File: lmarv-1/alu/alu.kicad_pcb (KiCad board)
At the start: 4 copper layers, 111.3 x 141 mm, 126 parts, among them J1 Conn_02x03_Odd_Even, J2 Conn_01x01, J3 Conn_01x01, J4 Conn_01x01, P1 dual-pcie-cardedge, Q1 DMP3056L, Q2 DMP3056L, Q3 DMP3056L, U1 74HC590, U10 74LVC541, U11 IS61LV256AL, U12 74LVC541, U13 74LVC541, U14 74LVC541, U15 IS61LV256AL, U16 IS61LV256AL, U17 74LVC541, U18 74LVC541, U19 74LVC541, U2 AT28BV64B-20JU, U20 IS61LV256AL, U21 74LVC541, U22 74LVC541, U23 74LVC541, U24 IS61LV256AL, U25 74LVC541, U26 74LVC541, U27 74LVC541, U28 IS61LV256AL, U29 74LVC541, U3 AT28BV256B-20JU, U30 74LVC541, U31 74LVC541, U32 IS61LV256AL, U33 74LVC541, U34 74LVC541, U35 74LVC541, U36 IS61LV256AL, U37 74LVC541, U38 74LVC541, U39 74LVC541, U4 74HC590, U40 IS61LV256AL, U41 74LVC541, U42 74LVC32, U43 74LVC04, U44 74LVC32, U45 74LVC541, U46 74LVC541, U47 74LVC541, U48 74LVC541, U49 74LVC541, U5 74LVC541, U50 74LVC541, U51 74LVC541, U52 74LVC541, U53 74LVC541, U54 74LVC541, U55 74LVC541, U56 74LVC541, U6 74LVC541, U7 74LVC541, U8 74LVC541, U9 74LVC541

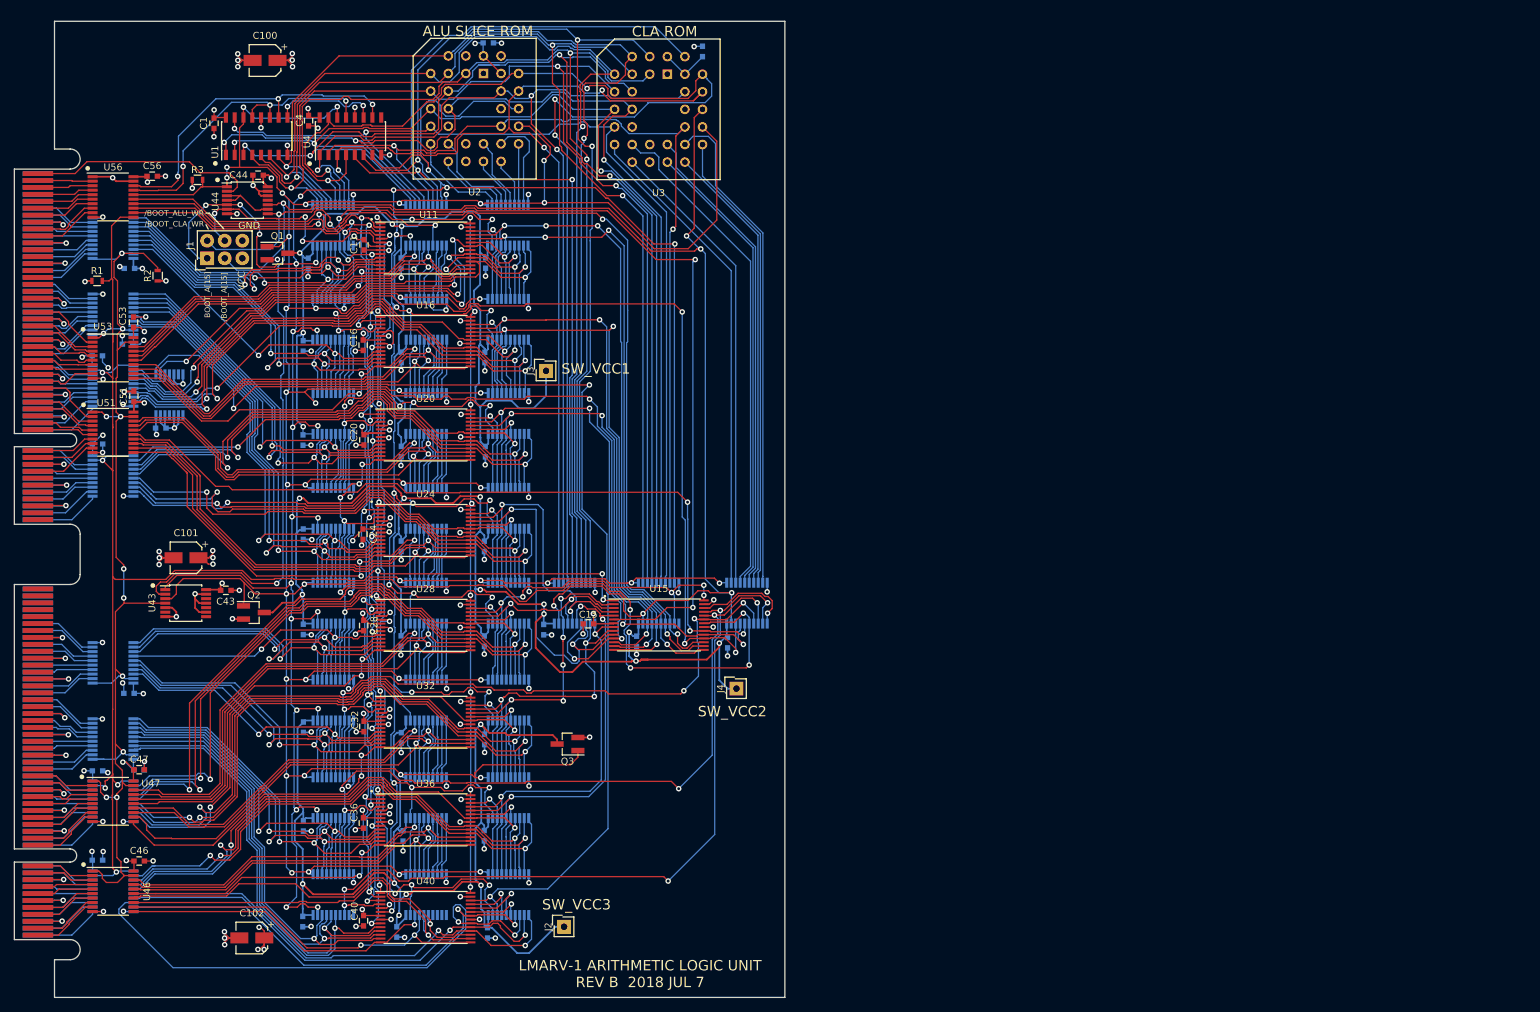
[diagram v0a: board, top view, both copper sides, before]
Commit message: Update alu.py, add some instruction diagrams
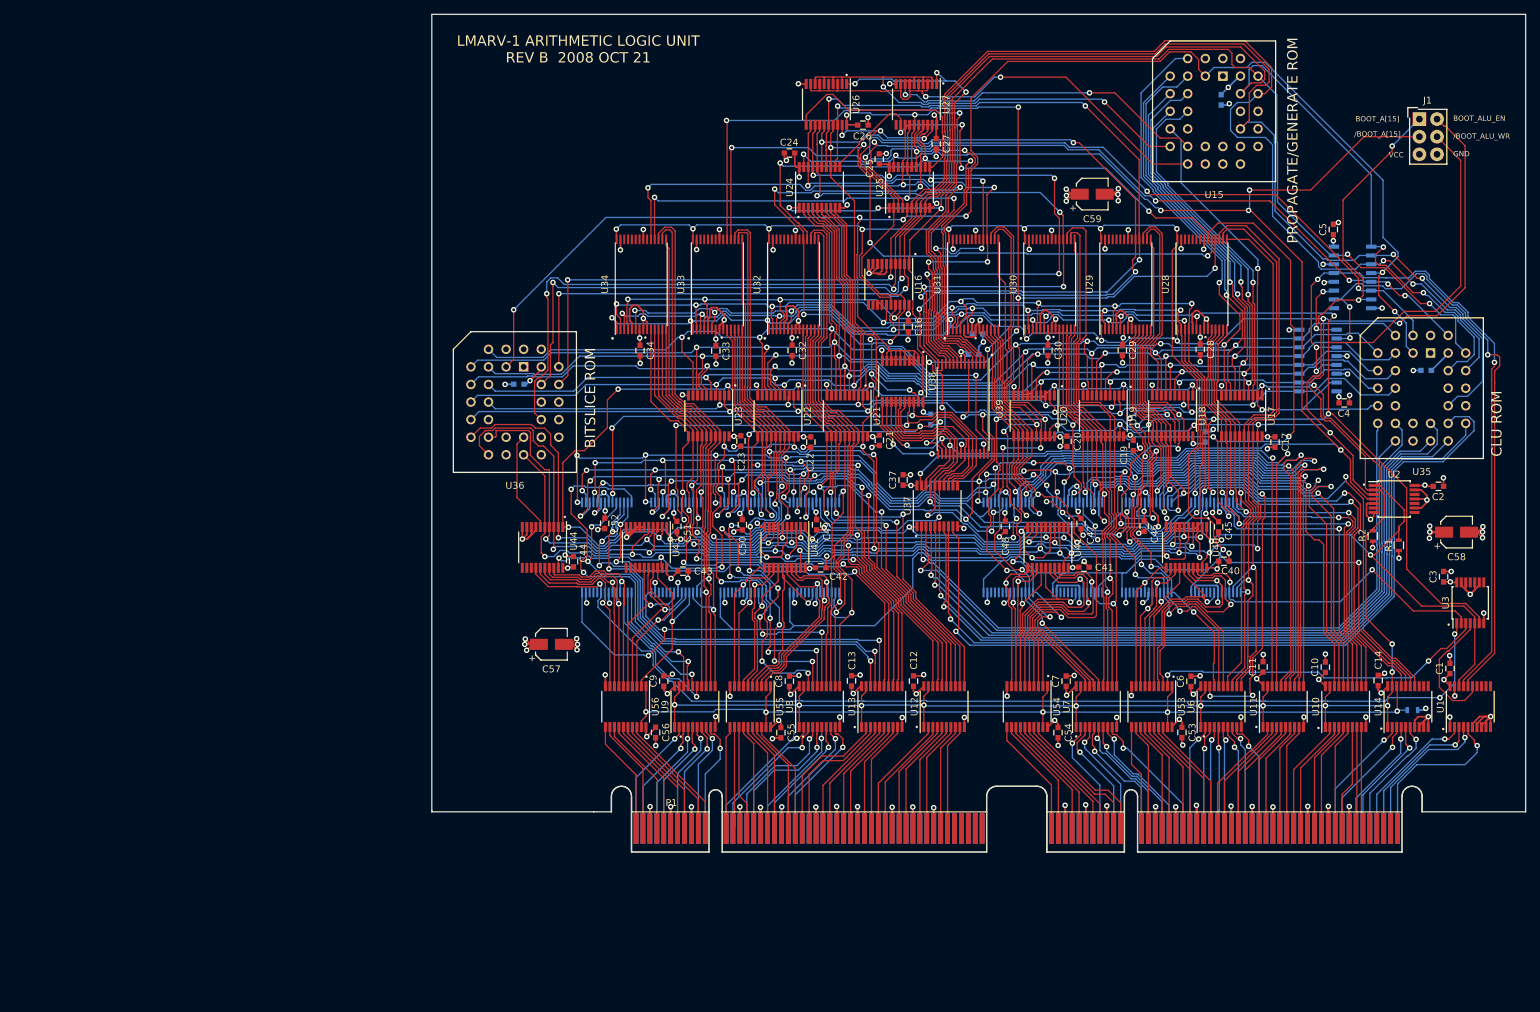
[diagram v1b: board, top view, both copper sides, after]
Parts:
- removed C100, C101, C102: 1u, Capacitors_SMD:CP_Elec_4x4.5
- removed J2, J3, J4: Conn_01x01, Connectors_Samtec:SL-101-X-XX_1x01
- removed Q1, Q2, Q3: DMP3056L, TO_SOT_Packages_SMD:SOT-23_Handsoldering
- added C57: 1u, Capacitors_SMD:CP_Elec_4x4.5, F.Cu at (81.3, 121.0)
- added C58: 1u, Capacitors_SMD:CP_Elec_4x4.5, F.Cu at (212.0, 104.8)
- added C59: 1u, Capacitors_SMD:CP_Elec_4x4.5, F.Cu at (159.4, 56.0)
- C1, C11, C16, C18, C20, C24, C28, C31, C32, C35, C38, C39, C4, C40, C43, C44, C46, C47, C51, C53, C56: value 0u1 -> 100n
- C10, C12, C13, C14, C17, C19, C2, C21, C22, C23, C25, C26, C27, C29, C3, C30, C33, C34, C37, C41, C42, C45, C48, C49, C5, C50, C52, C54, C55, C6, C7, C8, C9: value 0u1 -> 100n; moved to F.Cu
- C15, C36: value 0u1 -> 100n; moved to B.Cu
- P1: value dual-pcie-cardedge -> dual-pcie-cardedge_split; moved to F.Cu
- R3, U4: moved to B.Cu
- U1: value 74HC590 -> 74LVC541; footprint Housings_SOIC:SOIC-16_3.9x9.9mm_Pitch1.27mm -> Housings_SSOP:TSSOP-20_4.4x6.5mm_Pitch0.65mm
- U10, U12, U13, U25, U38, U6, U7, U8, U9: value 74LVC541 -> 74LVC541_a; moved to F.Cu
- U11, U24: value IS61LV256AL -> 74LVC541_a; footprint lmarv:TSOP-I-28_18.4x8mm_Pitch0.55mm -> Housings_SSOP:TSSOP-20_4.4x6.5mm_Pitch0.65mm
- U14, U17, U18, U19, U21, U22, U23, U26, U27, U37, U41, U54, U55: moved to F.Cu
- U15, U36: value IS61LV256AL -> AT28BV64B-20JU; footprint lmarv:TSOP-I-28_18.4x8mm_Pitch0.55mm -> Sockets:PLCC32
- U16, U20, U40: value IS61LV256AL -> 74LVC541; footprint lmarv:TSOP-I-28_18.4x8mm_Pitch0.55mm -> Housings_SSOP:TSSOP-20_4.4x6.5mm_Pitch0.65mm
- U2: value AT28BV64B-20JU -> 74LVC04; footprint Sockets:PLCC32 -> Housings_SSOP:TSSOP-14_4.4x5mm_Pitch0.65mm
- U29, U30, U31, U33, U34, U39: value 74LVC541 -> IS61LV256AL; footprint Housings_SSOP:TSSOP-20_4.4x6.5mm_Pitch0.65mm -> lmarv:TSOP-I-28_18.4x8mm_Pitch0.55mm; moved to F.Cu
- U3: value AT28BV256B-20JU -> 74LVC32; footprint Sockets:PLCC32 -> Housings_SSOP:TSSOP-14_4.4x5mm_Pitch0.65mm
- U35: value 74LVC541 -> AT28BV256B-20JU; footprint Housings_SSOP:TSSOP-20_4.4x6.5mm_Pitch0.65mm -> Sockets:PLCC32; moved to F.Cu
- U42: value 74LVC32 -> 74LVC541; footprint Housings_SSOP:TSSOP-14_4.4x5mm_Pitch0.65mm -> Housings_SSOP:TSSOP-20_4.4x6.5mm_Pitch0.65mm; moved to F.Cu
- U43: value 74LVC04 -> 74LVC541; footprint Housings_SSOP:TSSOP-14_4.4x5mm_Pitch0.65mm -> Housings_SSOP:TSSOP-20_4.4x6.5mm_Pitch0.65mm
- U44: value 74LVC32 -> 74LVC541; footprint Housings_SSOP:TSSOP-14_4.4x5mm_Pitch0.65mm -> Housings_SSOP:TSSOP-20_4.4x6.5mm_Pitch0.65mm
- U45, U48, U49, U50, U52: value 74LVC541 -> IS61LV256AL; footprint Housings_SSOP:TSSOP-20_4.4x6.5mm_Pitch0.65mm -> lmarv:TSOP-I-28_18.4x8mm_Pitch0.55mm
- U46, U47, U51: value 74LVC541 -> IS61LV256AL; footprint Housings_SSOP:TSSOP-20_4.4x6.5mm_Pitch0.65mm -> lmarv:TSOP-I-28_18.4x8mm_Pitch0.55mm; moved to B.Cu
- U5: value 74LVC541 -> 74HC590; footprint Housings_SSOP:TSSOP-20_4.4x6.5mm_Pitch0.65mm -> Housings_SOIC:SOIC-16_3.9x9.9mm_Pitch1.27mm
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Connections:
- C1 pad 2: GND -> GNDREF
- C10 pad 1: /SW_VCC2 -> VCC
- C10 pad 2: GND -> GNDREF
- C11 pad 2: GND -> GNDREF
- C12 pad 1: /SW_VCC1 -> VCC
- C12 pad 2: GND -> GNDREF
- C13 pad 1: /SW_VCC1 -> VCC
- C13 pad 2: GND -> GNDREF
- C14 pad 1: /SW_VCC1 -> VCC
- C14 pad 2: GND -> GNDREF
- C15 pad 2: GND -> GNDREF
- C16 pad 2: GND -> GNDREF
- C17 pad 1: /SW_VCC1 -> VCC
- C17 pad 2: GND -> GNDREF
- C18 pad 1: /SW_VCC1 -> VCC
- C18 pad 2: GND -> GNDREF
- C19 pad 1: /SW_VCC1 -> VCC
- C19 pad 2: GND -> GNDREF
- C2 pad 2: GND -> GNDREF
- C20 pad 2: GND -> GNDREF
- C21 pad 1: /SW_VCC2 -> VCC
- C21 pad 2: GND -> GNDREF
- C22 pad 1: /SW_VCC2 -> VCC
- C22 pad 2: GND -> GNDREF
- C23 pad 1: /SW_VCC2 -> VCC
- C23 pad 2: GND -> GNDREF
- C24 pad 2: GND -> GNDREF
- C25 pad 1: /SW_VCC2 -> VCC
- C25 pad 2: GND -> GNDREF
- C26 pad 1: /SW_VCC2 -> VCC
- C26 pad 2: GND -> GNDREF
- C27 pad 1: /SW_VCC2 -> VCC
- C27 pad 2: GND -> GNDREF
- C28 pad 2: GND -> GNDREF
- C29 pad 1: /SW_VCC3 -> VCC
- C29 pad 2: GND -> GNDREF
- C3 pad 2: GND -> GNDREF
- C30 pad 1: /SW_VCC3 -> VCC
- C30 pad 2: GND -> GNDREF
- C31 pad 1: /SW_VCC3 -> VCC
- C31 pad 2: GND -> GNDREF
- C32 pad 2: GND -> GNDREF
- C33 pad 1: /SW_VCC3 -> VCC
- C33 pad 2: GND -> GNDREF
- C34 pad 1: /SW_VCC3 -> VCC
- C34 pad 2: GND -> GNDREF
- C35 pad 1: /SW_VCC3 -> VCC
- C35 pad 2: GND -> GNDREF
- C36 pad 2: GND -> GNDREF
- C37 pad 1: /SW_VCC3 -> VCC
- C37 pad 2: GND -> GNDREF
- C38 pad 1: /SW_VCC3 -> VCC
- C38 pad 2: GND -> GNDREF
- C39 pad 1: /SW_VCC3 -> VCC
- C39 pad 2: GND -> GNDREF
- C4 pad 2: GND -> GNDREF
- C40 pad 2: GND -> GNDREF
- C41 pad 2: GND -> GNDREF
- C42 pad 2: GND -> GNDREF
- C43 pad 2: GND -> GNDREF
- C44 pad 2: GND -> GNDREF
- C45 pad 2: GND -> GNDREF
- C46 pad 2: GND -> GNDREF
- C47 pad 2: GND -> GNDREF
- C48 pad 2: GND -> GNDREF
- C49 pad 2: GND -> GNDREF
- C5 pad 1: /SW_VCC1 -> VCC
- C5 pad 2: GND -> GNDREF
- C50 pad 2: GND -> GNDREF
- C51 pad 2: GND -> GNDREF
- C52 pad 2: GND -> GNDREF
- C53 pad 2: GND -> GNDREF
- C54 pad 2: GND -> GNDREF
- C55 pad 2: GND -> GNDREF
- C56 pad 2: GND -> GNDREF
- C6 pad 1: /SW_VCC1 -> VCC
- C6 pad 2: GND -> GNDREF
- C7 pad 1: /SW_VCC1 -> VCC
- C7 pad 2: GND -> GNDREF
- C8 pad 1: /SW_VCC2 -> VCC
- C8 pad 2: GND -> GNDREF
- C9 pad 1: /SW_VCC2 -> VCC
- C9 pad 2: GND -> GNDREF
- J1 pad 2: /~BOOT_CLA_WR -> /BOOT_ALU_EN
- J1 pad 6: GND -> GNDREF
- P1 pad 101: GND -> GNDREF
- P1 pad 107: GND -> GNDREF
- P1 pad 112: GND -> GNDREF
- P1 pad 118: GND -> GNDREF
- P1 pad 123: GND -> GNDREF
- P1 pad 129: GND -> GNDREF
- P1 pad 134: GND -> GNDREF
- P1 pad 14: GND -> GNDREF
- P1 pad 140: GND -> GNDREF
- P1 pad 150: GND -> GNDREF
- P1 pad 156: GND -> GNDREF
- P1 pad 161: GND -> GNDREF
- P1 pad 167: GND -> GNDREF
- P1 pad 172: GND -> GNDREF
- P1 pad 178: GND -> GNDREF
- P1 pad 183: GND -> GNDREF
- P1 pad 189: GND -> GNDREF
- P1 pad 196: /~BOOT_WR -> /~BOOT_WR'
- P1 pad 20: GND -> GNDREF
- P1 pad 25: GND -> GNDREF
- P1 pad 3: GND -> GNDREF
- P1 pad 31: GND -> GNDREF
- P1 pad 36: GND -> GNDREF
- P1 pad 42: GND -> GNDREF
- P1 pad 52: GND -> GNDREF
- P1 pad 58: GND -> GNDREF
- P1 pad 63: GND -> GNDREF
- P1 pad 69: GND -> GNDREF
- P1 pad 74: GND -> GNDREF
- P1 pad 80: GND -> GNDREF
- P1 pad 85: GND -> GNDREF
- P1 pad 9: GND -> GNDREF
- P1 pad 91: GND -> GNDREF
- R1 pad 2: /~alu_oe -> /~BOOT_ALU_EN
- R2 pad 1: VCC -> /BOOT_ALU_EN
- R2 pad 2: /BOOT_ALU_EN -> GNDREF
- R3 pad 2: /~BOOT_ALU_EN -> /~alu_oe
- U1 pad 1: /BOOT_A[1] -> GNDREF
- U1 pad 10: /~BOOT_RST -> GNDREF
- U1 pad 11: /BOOT_CLK -> Net-(U1-Pad11)
- U1 pad 12: GND -> Net-(U1-Pad12)
- U1 pad 13: /BOOT_CLK -> Net-(U1-Pad13)
- U1 pad 14: /~BOOT_ALU_EN -> Net-(U1-Pad14)
- U1 pad 15: /BOOT_A[0] -> /~BOOT_WR
- U1 pad 16: VCC -> /~BOOT_RST
- U1 pad 2: /BOOT_A[2] -> /~BOOT_ALU_EN'
- U1 pad 3: /BOOT_A[3] -> /BOOT_CLK'
- U1 pad 4: /BOOT_A[4] -> /~BOOT_RST'
- U1 pad 5: /BOOT_A[5] -> /~BOOT_WR'
- U1 pad 6: /BOOT_A[6] -> GNDREF
- U1 pad 7: /BOOT_A[7] -> GNDREF
- U1 pad 8: GND -> GNDREF
- U1 pad 9: /~BOOT_RCO -> GNDREF
- U10 pad 1: /~BOOT_ALU_EN -> /BOOT_ALU_EN
- U10 pad 10: GND -> GNDREF
- U10 pad 11: Net-(U10-Pad11) -> /rs2b[0]
- U10 pad 12: /cin[7] -> /rs2b[1]
- U10 pad 13: /cin[6] -> /rs2b[2]
- U10 pad 14: /cin[5] -> /rs2b[3]
- U10 pad 15: /cin[4] -> /rs2b[4]
- U10 pad 16: /cin[3] -> /rs2b[5]
- U10 pad 17: /cin[2] -> /rs2b[6]
- U10 pad 18: /cin[1] -> /rs2b[7]
- U10 pad 19: /~BOOT_A[15] -> /BOOT_ALU_EN
- U10 pad 2: /CLA_D0 -> /rs2[7]
- U10 pad 20: /SW_VCC2 -> VCC
- U10 pad 3: /CLA_D1 -> /rs2[6]
- U10 pad 4: /CLA_D2 -> /rs2[5]
- U10 pad 5: /CLA_D3 -> /rs2[4]
- U10 pad 6: /CLA_D4 -> /rs2[3]
- U10 pad 7: /CLA_D5 -> /rs2[2]
- U10 pad 8: /CLA_D6 -> /rs2[1]
- U10 pad 9: /CLA_D7 -> /rs2[0]
- U11 pad 1: GND -> /BOOT_ALU_EN
- U11 pad 10: /rs1b[0] -> GNDREF
- U11 pad 11: /rdb[0]' -> /rs2b[8]
- U11 pad 12: /rdb[1] -> /rs2b[9]
- U11 pad 13: /rdb[2] -> /rs2b[10]
- U11 pad 14: GND -> /rs2b[11]
- U11 pad 15: /rdb[3] -> /rs2b[12]
- U11 pad 16: /cout[0] -> /rs2b[13]
- U11 pad 17: /p[0] -> /rs2b[14]
- U11 pad 18: /g[0] -> /rs2b[15]
- U11 pad 19: /lt[0] -> /BOOT_ALU_EN
- U11 pad 2: /alu_f[3] -> /rs2[15]
- U11 pad 20: GND -> VCC
- U11 pad 3: /rs2b[3] -> /rs2[14]
- U11 pad 4: /rs2b[2] -> /rs2[13]
- U11 pad 5: /rs2b[1] -> /rs2[12]
- U11 pad 6: /rs2b[0] -> /rs2[11]
- U11 pad 7: /rs1b[3] -> /rs2[10]
- U11 pad 8: /rs1b[2] -> /rs2[9]
- U11 pad 9: /rs1b[1] -> /rs2[8]
- U12 pad 1: /~BOOT_ALU_EN -> /BOOT_ALU_EN
- U12 pad 10: GND -> GNDREF
- U12 pad 11: Net-(U12-Pad11) -> /rs2b[16]
- U12 pad 12: Net-(U12-Pad12) -> /rs2b[17]
- U12 pad 13: /cin[1] -> /rs2b[18]
- U12 pad 14: Net-(U12-Pad14) -> /rs2b[19]
- U12 pad 15: /rs2b[7] -> /rs2b[20]
- U12 pad 16: /rs2b[6] -> /rs2b[21]
- U12 pad 17: /rs2b[5] -> /rs2b[22]
- U12 pad 18: /rs2b[4] -> /rs2b[23]
- U12 pad 19: /BOOT_A[15] -> /BOOT_ALU_EN
- U12 pad 2: /rs2b[0] -> /rs2[23]
- U12 pad 20: /SW_VCC1 -> VCC
- U12 pad 3: /rs2b[1] -> /rs2[22]
- U12 pad 4: /rs2b[2] -> /rs2[21]
- U12 pad 5: /rs2b[3] -> /rs2[20]
- U12 pad 6: GND -> /rs2[19]
- U12 pad 7: /cin[0] -> /rs2[18]
- U12 pad 8: GND -> /rs2[17]
- U12 pad 9: GND -> /rs2[16]
- U13 pad 1: /~BOOT_ALU_EN -> /BOOT_ALU_EN
- U13 pad 10: GND -> GNDREF
- U13 pad 11: Net-(U13-Pad11) -> /rs2b[24]
- U13 pad 12: Net-(U13-Pad12) -> /rs2b[25]
- U13 pad 13: Net-(U13-Pad13) -> /rs2b[26]
- U13 pad 14: Net-(U13-Pad14) -> /rs2b[27]
- U13 pad 15: /rs1b[4] -> /rs2b[28]
- U13 pad 16: /rs1b[5] -> /rs2b[29]
- U13 pad 17: /rs1b[6] -> /rs2b[30]
- U13 pad 18: /rs1b[7] -> /rs2b[31]
- U13 pad 19: /BOOT_A[15] -> /BOOT_ALU_EN
- U13 pad 2: /rs1b[3] -> /rs2[31]
- U13 pad 20: /SW_VCC1 -> VCC
- U13 pad 3: /rs1b[2] -> /rs2[30]
- U13 pad 4: /rs1b[1] -> /rs2[29]
- U13 pad 5: /rs1b[0] -> /rs2[28]
- U13 pad 6: GND -> /rs2[27]
- U13 pad 7: Net-(U13-Pad7) -> /rs2[26]
- U13 pad 8: Net-(U13-Pad8) -> /rs2[25]
- U13 pad 9: Net-(U13-Pad9) -> /rs2[24]
- U14 pad 1: /~BOOT_ALU_EN -> /BOOT_ALU_EN
- U14 pad 10: GND -> GNDREF
- U14 pad 11: /rdb[4] -> Net-(U14-Pad11)
- U14 pad 12: /rdb[5] -> Net-(U14-Pad12)
- U14 pad 13: /rdb[6] -> Net-(U14-Pad13)
- U14 pad 14: /rdb[7] -> /alu_f[3]
- U14 pad 15: /cout[1] -> /alu_f[2]
- U14 pad 16: /p[1] -> /alu_f[1]
- U14 pad 17: /g[1] -> /alu_f[0]
- U14 pad 18: /lt[1] -> /~alu_oe
- U14 pad 19: /BOOT_A[15] -> /BOOT_ALU_EN
- U14 pad 2: /lt[0] -> /~alu_oe'
- U14 pad 20: /SW_VCC1 -> VCC
- U14 pad 3: /g[0] -> /f[0]
- U14 pad 4: /p[0] -> /f[1]
- U14 pad 5: /cout[0] -> /f[2]
- U14 pad 6: /rdb[3] -> /f[3]
- U14 pad 7: /rdb[2] -> GNDREF
- U14 pad 8: /rdb[1] -> GNDREF
- U14 pad 9: /rdb[0]' -> GNDREF
- U15 pad 1: /g[6] -> Net-(U15-Pad1)
- U15 pad 10: /cin[0] -> /BOOT_A[1]
- U15 pad 11: /cin[1] -> /BOOT_A[0]
- U15 pad 12: /cin[2] -> Net-(U15-Pad12)
- U15 pad 13: /cin[3] -> /SLICE1_G
- U15 pad 14: GND -> /SLICE1_P
- U15 pad 15: /cin[4] -> /SLICE1_CIN
- U15 pad 16: /cin[5] -> GNDREF
- U15 pad 17: /cin[6] -> Net-(U15-Pad17)
- U15 pad 18: /cin[7] -> Net-(U15-Pad18)
- U15 pad 19: Net-(U10-Pad11) -> Net-(U15-Pad19)
- U15 pad 2: /g[5] -> Net-(U15-Pad2)
- U15 pad 20: GND -> Net-(U15-Pad20)
- U15 pad 21: /g[4] -> Net-(U15-Pad21)
- U15 pad 22: /~alu_oe -> Net-(U15-Pad22)
- U15 pad 23: /p[5] -> GNDREF
- U15 pad 24: /p[4] -> /BOOT_A[10]
- U15 pad 25: /g[3] -> GNDREF
- U15 pad 26: /p[6] -> Net-(U15-Pad26)
- U15 pad 27: /~BOOT_CLA_WR -> /BOOT_A[11]
- U15 pad 28: VCC -> /BOOT_A[9]
- U15 pad 3: /p[3] -> /BOOT_A[12]
- U15 pad 4: /g[2] -> /BOOT_A[7]
- U15 pad 5: /p[2] -> /BOOT_A[6]
- U15 pad 6: /g[1] -> /BOOT_A[5]
- U15 pad 7: /p[1] -> /BOOT_A[4]
- U15 pad 8: /g[0] -> /BOOT_A[3]
- U15 pad 9: /p[0] -> /BOOT_A[2]
- U16 pad 1: GND -> /~BOOT_ALU_EN
- U16 pad 10: /rs1b[4] -> GNDREF
- U16 pad 11: /rdb[4] -> Net-(U16-Pad11)
- U16 pad 12: /rdb[5] -> Net-(U16-Pad12)
- U16 pad 13: /rdb[6] -> Net-(U16-Pad13)
- U16 pad 14: GND -> Net-(U16-Pad14)
- U16 pad 15: /rdb[7] -> /alu_f[3]
- U16 pad 16: /cout[1] -> /alu_f[2]
- U16 pad 17: /p[1] -> /alu_f[1]
- U16 pad 18: /g[1] -> /alu_f[0]
- U16 pad 19: /lt[1] -> /BOOT_A[15]
- U16 pad 2: /alu_f[3] -> /BOOT_A[8]
- U16 pad 20: GND -> VCC
- U16 pad 3: /rs2b[7] -> /BOOT_A[9]
- U16 pad 4: /rs2b[6] -> /BOOT_A[10]
- U16 pad 5: /rs2b[5] -> /BOOT_A[11]
- U16 pad 6: /rs2b[4] -> GNDREF
- U16 pad 7: /rs1b[7] -> GNDREF
- U16 pad 8: /rs1b[6] -> GNDREF
- U16 pad 9: /rs1b[5] -> GNDREF
- U17 pad 10: GND -> GNDREF
- U17 pad 11: Net-(U17-Pad11) -> /rs2b[3]
- U17 pad 12: Net-(U17-Pad12) -> /rs2b[2]
- U17 pad 13: /cin[2] -> /rs2b[1]
- U17 pad 14: Net-(U17-Pad14) -> /rs2b[0]
- U17 pad 15: /rs2b[11] -> /rs1b[3]
- U17 pad 16: /rs2b[10] -> /rs1b[2]
- U17 pad 17: /rs2b[9] -> /rs1b[1]
- U17 pad 18: /rs2b[8] -> /rs1b[0]
- U17 pad 2: /rs2b[4] -> /BOOT_A[0]
- U17 pad 20: /SW_VCC1 -> VCC
- U17 pad 3: /rs2b[5] -> /BOOT_A[1]
- U17 pad 4: /rs2b[6] -> /BOOT_A[2]
- U17 pad 5: /rs2b[7] -> /BOOT_A[3]
- U17 pad 6: Net-(U12-Pad14) -> /BOOT_A[4]
- U17 pad 7: /cin[1] -> /BOOT_A[5]
- U17 pad 8: Net-(U12-Pad12) -> /BOOT_A[6]
- U17 pad 9: Net-(U12-Pad11) -> /BOOT_A[7]
- U18 pad 10: GND -> GNDREF
- U18 pad 11: Net-(U18-Pad11) -> /rs2b[7]
- U18 pad 12: Net-(U18-Pad12) -> /rs2b[6]
- U18 pad 13: Net-(U18-Pad13) -> /rs2b[5]
- U18 pad 14: Net-(U18-Pad14) -> /rs2b[4]
- U18 pad 15: /rs1b[8] -> /rs1b[7]
- U18 pad 16: /rs1b[9] -> /rs1b[6]
- U18 pad 17: /rs1b[10] -> /rs1b[5]
- U18 pad 18: /rs1b[11] -> /rs1b[4]
- U18 pad 2: /rs1b[7] -> /BOOT_A[0]
- U18 pad 20: /SW_VCC1 -> VCC
- U18 pad 3: /rs1b[6] -> /BOOT_A[1]
- U18 pad 4: /rs1b[5] -> /BOOT_A[2]
- U18 pad 5: /rs1b[4] -> /BOOT_A[3]
- U18 pad 6: Net-(U13-Pad14) -> /BOOT_A[4]
- U18 pad 7: Net-(U13-Pad13) -> /BOOT_A[5]
- U18 pad 8: Net-(U13-Pad12) -> /BOOT_A[6]
- U18 pad 9: Net-(U13-Pad11) -> /BOOT_A[7]
- U19 pad 10: GND -> GNDREF
- U19 pad 11: /rdb[8] -> /rs2b[11]
- U19 pad 12: /rdb[9] -> /rs2b[10]
- U19 pad 13: /rdb[10] -> /rs2b[9]
- U19 pad 14: /rdb[11] -> /rs2b[8]
- U19 pad 15: /cout[2] -> /rs1b[11]
- U19 pad 16: /p[2] -> /rs1b[10]
- U19 pad 17: /g[2] -> /rs1b[9]
- U19 pad 18: /lt[2] -> /rs1b[8]
- U19 pad 2: /lt[1] -> /BOOT_A[0]
- U19 pad 20: /SW_VCC1 -> VCC
- U19 pad 3: /g[1] -> /BOOT_A[1]
- U19 pad 4: /p[1] -> /BOOT_A[2]
- U19 pad 5: /cout[1] -> /BOOT_A[3]
- U19 pad 6: /rdb[7] -> /BOOT_A[4]
- U19 pad 7: /rdb[6] -> /BOOT_A[5]
- U19 pad 8: /rdb[5] -> /BOOT_A[6]
- U19 pad 9: /rdb[4] -> /BOOT_A[7]
- U2 pad 1: Net-(U2-Pad1) -> /~BOOT_ALU_EN
- U2 pad 10: /BOOT_A[1] -> Net-(U2-Pad10)
- U2 pad 11: /BOOT_A[0] -> GNDREF
- U2 pad 13: /SLICE_D0 -> GNDREF
- U2 pad 14: /SLICE_D1 -> VCC
- U2 pad 2: Net-(U2-Pad2) -> /BOOT_ALU_EN
- U2 pad 3: /BOOT_A[12] -> /BOOT_A[15]
- U2 pad 4: /BOOT_A[7] -> /~BOOT_A[15]
- U2 pad 5: /BOOT_A[6] -> GNDREF
- U2 pad 6: /BOOT_A[5] -> Net-(U2-Pad6)
- U2 pad 7: /BOOT_A[4] -> GNDREF
- U2 pad 8: /BOOT_A[3] -> Net-(U2-Pad8)
- U2 pad 9: /BOOT_A[2] -> GNDREF
- U20 pad 1: GND -> /~BOOT_ALU_EN
- U20 pad 10: /rs1b[8] -> GNDREF
- U20 pad 11: /rdb[8] -> /rs2b[15]
- U20 pad 12: /rdb[9] -> /rs2b[14]
- U20 pad 13: /rdb[10] -> /rs2b[13]
- U20 pad 14: GND -> /rs2b[12]
- U20 pad 15: /rdb[11] -> /rs1b[15]
- U20 pad 16: /cout[2] -> /rs1b[14]
- U20 pad 17: /p[2] -> /rs1b[13]
- U20 pad 18: /g[2] -> /rs1b[12]
- U20 pad 19: /lt[2] -> /BOOT_A[15]
- U20 pad 2: /alu_f[3] -> /BOOT_A[0]
- U20 pad 20: GND -> VCC
- U20 pad 3: /rs2b[11] -> /BOOT_A[1]
- U20 pad 4: /rs2b[10] -> /BOOT_A[2]
- U20 pad 5: /rs2b[9] -> /BOOT_A[3]
- U20 pad 6: /rs2b[8] -> /BOOT_A[4]
- U20 pad 7: /rs1b[11] -> /BOOT_A[5]
- U20 pad 8: /rs1b[10] -> /BOOT_A[6]
- U20 pad 9: /rs1b[9] -> /BOOT_A[7]
- U21 pad 10: GND -> GNDREF
- U21 pad 11: Net-(U21-Pad11) -> /rs2b[19]
- U21 pad 12: Net-(U21-Pad12) -> /rs2b[18]
- U21 pad 13: /cin[3] -> /rs2b[17]
- U21 pad 14: Net-(U21-Pad14) -> /rs2b[16]
- U21 pad 15: /rs2b[15] -> /rs1b[19]
- U21 pad 16: /rs2b[14] -> /rs1b[18]
- U21 pad 17: /rs2b[13] -> /rs1b[17]
- U21 pad 18: /rs2b[12] -> /rs1b[16]
- U21 pad 2: /rs2b[8] -> /BOOT_A[0]
- U21 pad 20: /SW_VCC2 -> VCC
- U21 pad 3: /rs2b[9] -> /BOOT_A[1]
- U21 pad 4: /rs2b[10] -> /BOOT_A[2]
- U21 pad 5: /rs2b[11] -> /BOOT_A[3]
- U21 pad 6: Net-(U17-Pad14) -> /BOOT_A[4]
- U21 pad 7: /cin[2] -> /BOOT_A[5]
- U21 pad 8: Net-(U17-Pad12) -> /BOOT_A[6]
- U21 pad 9: Net-(U17-Pad11) -> /BOOT_A[7]
- U22 pad 10: GND -> GNDREF
- U22 pad 11: Net-(U22-Pad11) -> /rs2b[23]
- U22 pad 12: Net-(U22-Pad12) -> /rs2b[22]
- U22 pad 13: Net-(U22-Pad13) -> /rs2b[21]
- U22 pad 14: Net-(U22-Pad14) -> /rs2b[20]
- U22 pad 15: /rs1b[12] -> /rs1b[23]
- U22 pad 16: /rs1b[13] -> /rs1b[22]
- U22 pad 17: /rs1b[14] -> /rs1b[21]
- U22 pad 18: /rs1b[15] -> /rs1b[20]
- U22 pad 2: /rs1b[11] -> /BOOT_A[0]
- U22 pad 20: /SW_VCC2 -> VCC
- U22 pad 3: /rs1b[10] -> /BOOT_A[1]
- U22 pad 4: /rs1b[9] -> /BOOT_A[2]
- U22 pad 5: /rs1b[8] -> /BOOT_A[3]
- U22 pad 6: Net-(U18-Pad14) -> /BOOT_A[4]
- U22 pad 7: Net-(U18-Pad13) -> /BOOT_A[5]
- U22 pad 8: Net-(U18-Pad12) -> /BOOT_A[6]
- U22 pad 9: Net-(U18-Pad11) -> /BOOT_A[7]
- U23 pad 10: GND -> GNDREF
- U23 pad 11: /rdb[12] -> /rs2b[27]
- U23 pad 12: /rdb[13] -> /rs2b[26]
- U23 pad 13: /rdb[14] -> /rs2b[25]
- U23 pad 14: /rdb[15] -> /rs2b[24]
- U23 pad 15: /cout[3] -> /rs1b[27]
- U23 pad 16: /p[3] -> /rs1b[26]
- U23 pad 17: /g[3] -> /rs1b[25]
- U23 pad 18: /lt[3] -> /rs1b[24]
- U23 pad 2: /lt[2] -> /BOOT_A[0]
- U23 pad 20: /SW_VCC2 -> VCC
- U23 pad 3: /g[2] -> /BOOT_A[1]
- U23 pad 4: /p[2] -> /BOOT_A[2]
- U23 pad 5: /cout[2] -> /BOOT_A[3]
- U23 pad 6: /rdb[11] -> /BOOT_A[4]
- U23 pad 7: /rdb[10] -> /BOOT_A[5]
- U23 pad 8: /rdb[9] -> /BOOT_A[6]
- U23 pad 9: /rdb[8] -> /BOOT_A[7]
- U24 pad 1: GND -> /~BOOT_ALU_EN
- U24 pad 10: /rs1b[12] -> GNDREF
- U24 pad 11: /rdb[12] -> /cin[0]
- U24 pad 12: /rdb[13] -> /g[0]
- U24 pad 13: /rdb[14] -> /p[0]
- U24 pad 14: GND -> /g[1]
- U24 pad 15: /rdb[15] -> /p[1]
- U24 pad 16: /cout[3] -> /g[2]
- U24 pad 17: /p[3] -> /p[2]
- U24 pad 19: /lt[3] -> /~BOOT_A[15]
- U24 pad 2: /alu_f[3] -> /BOOT_A[7]
- U24 pad 20: GND -> VCC
- U24 pad 3: /rs2b[15] -> /BOOT_A[6]
- U24 pad 4: /rs2b[14] -> /BOOT_A[5]
- U24 pad 5: /rs2b[13] -> /BOOT_A[4]
- U24 pad 6: /rs2b[12] -> /BOOT_A[3]
- U24 pad 7: /rs1b[15] -> /BOOT_A[2]
- U24 pad 8: /rs1b[14] -> /BOOT_A[1]
- U24 pad 9: /rs1b[13] -> /BOOT_A[0]
- U25 pad 10: GND -> GNDREF
- U25 pad 11: Net-(U25-Pad11) -> /p[3]
- U25 pad 12: Net-(U25-Pad12) -> /g[4]
- U25 pad 13: /cin[4] -> /p[4]
- U25 pad 14: Net-(U25-Pad14) -> /g[5]
- U25 pad 15: /rs2b[19] -> /p[5]
- U25 pad 16: /rs2b[18] -> /g[6]
- U25 pad 17: /rs2b[17] -> /p[6]
- U25 pad 18: /rs2b[16] -> Net-(U25-Pad18)
- U25 pad 19: /BOOT_A[15] -> /~BOOT_A[15]
- U25 pad 2: /rs2b[12] -> /BOOT_A[15]
- U25 pad 20: /SW_VCC2 -> VCC
- U25 pad 3: /rs2b[13] -> /BOOT_A[14]
- U25 pad 4: /rs2b[14] -> /BOOT_A[13]
- U25 pad 5: /rs2b[15] -> /BOOT_A[12]
- U25 pad 6: Net-(U21-Pad14) -> /BOOT_A[11]
- U25 pad 7: /cin[3] -> /BOOT_A[10]
- U25 pad 8: Net-(U21-Pad12) -> /BOOT_A[9]
- U25 pad 9: Net-(U21-Pad11) -> /BOOT_A[8]
- U26 pad 10: GND -> GNDREF
- U26 pad 11: Net-(U26-Pad11) -> /p[3]
- U26 pad 12: Net-(U26-Pad12) -> /g[3]
- U26 pad 13: Net-(U26-Pad13) -> /p[2]
- U26 pad 14: Net-(U26-Pad14) -> /g[2]
- U26 pad 15: /rs1b[16] -> /p[1]
- U26 pad 16: /rs1b[17] -> /g[1]
- U26 pad 17: /rs1b[18] -> /p[0]
- U26 pad 18: /rs1b[19] -> /g[0]
- U26 pad 2: /rs1b[15] -> /SLICE1_G
- U26 pad 20: /SW_VCC2 -> VCC
- U26 pad 3: /rs1b[14] -> /SLICE1_P
- U26 pad 4: /rs1b[13] -> /SLICE1_G
- U26 pad 5: /rs1b[12] -> /SLICE1_P
- U26 pad 6: Net-(U22-Pad14) -> /SLICE1_G
- U26 pad 7: Net-(U22-Pad13) -> /SLICE1_P
- U26 pad 8: Net-(U22-Pad12) -> /SLICE1_G
- U26 pad 9: Net-(U22-Pad11) -> /SLICE1_P
- U27 pad 10: GND -> GNDREF
- U27 pad 11: /rdb[16] -> Net-(U27-Pad11)
- U27 pad 12: /rdb[17] -> /cin[0]
- U27 pad 13: /rdb[18] -> /p[6]
- U27 pad 14: /rdb[19] -> /g[6]
- U27 pad 15: /cout[4] -> /p[5]
- U27 pad 16: /p[4] -> /g[5]
- U27 pad 17: /g[4] -> /p[4]
- U27 pad 18: /lt[4] -> /g[4]
- U27 pad 2: /lt[3] -> /SLICE1_G
- U27 pad 20: /SW_VCC2 -> VCC
- U27 pad 3: /g[3] -> /SLICE1_P
- U27 pad 4: /p[3] -> /SLICE1_G
- U27 pad 5: /cout[3] -> /SLICE1_P
- U27 pad 6: /rdb[15] -> /SLICE1_G
- U27 pad 7: /rdb[14] -> /SLICE1_P
- U27 pad 8: /rdb[13] -> /SLICE1_CIN
- U27 pad 9: /rdb[12] -> /SLICE1_P
- U28 pad 1: GND -> GNDREF
- U28 pad 10: /rs1b[16] -> /rs1b[0]
- U28 pad 11: /rdb[16] -> /g[0]
- U28 pad 12: /rdb[17] -> /p[0]
- U28 pad 13: /rdb[18] -> /cin[0]
- U28 pad 14: GND -> GNDREF
- U28 pad 15: /rdb[19] -> Net-(U28-Pad15)
- U28 pad 16: /cout[4] -> Net-(U28-Pad16)
- U28 pad 17: /p[4] -> Net-(U28-Pad17)
- U28 pad 18: /g[4] -> Net-(U28-Pad18)
- U28 pad 19: /lt[4] -> Net-(U28-Pad19)
- U28 pad 2: /alu_f[3] -> GNDREF
- U28 pad 20: GND -> GNDREF
- U28 pad 21: /alu_f[1] -> /alu_f[2]
- U28 pad 22: /~alu_oe -> /BOOT_ALU_EN
- U28 pad 23: /alu_f[2] -> /alu_f[3]
- U28 pad 24: /alu_f[0] -> /alu_f[1]
- U28 pad 25: /cin[4] -> /alu_f[0]
- U28 pad 26: GND -> GNDREF
- U28 pad 3: /rs2b[19] -> /rs2b[3]
- U28 pad 4: /rs2b[18] -> /rs2b[2]
- U28 pad 5: /rs2b[17] -> /rs2b[1]
- U28 pad 6: /rs2b[16] -> /rs2b[0]
- U28 pad 7: /rs1b[19] -> /rs1b[3]
- U28 pad 8: /rs1b[18] -> /rs1b[2]
- U28 pad 9: /rs1b[17] -> /rs1b[1]
- U29 pad 1: /~BOOT_ALU_EN -> GNDREF
- U29 pad 10: GND -> /rs1b[4]
- U29 pad 11: Net-(U29-Pad11) -> /g[1]
- U29 pad 12: Net-(U29-Pad12) -> /p[1]
- U29 pad 13: /cin[5] -> Net-(U29-Pad13)
- U29 pad 14: Net-(U29-Pad14) -> GNDREF
- U29 pad 15: /rs2b[23] -> Net-(U29-Pad15)
- U29 pad 16: /rs2b[22] -> Net-(U29-Pad16)
- U29 pad 17: /rs2b[21] -> Net-(U29-Pad17)
- U29 pad 18: /rs2b[20] -> Net-(U29-Pad18)
- U29 pad 19: /BOOT_A[15] -> Net-(U29-Pad19)
- U29 pad 2: /rs2b[16] -> GNDREF
- U29 pad 20: /SW_VCC3 -> GNDREF
- U29 pad 3: /rs2b[17] -> /rs2b[7]
- U29 pad 4: /rs2b[18] -> /rs2b[6]
- U29 pad 5: /rs2b[19] -> /rs2b[5]
- U29 pad 6: Net-(U25-Pad14) -> /rs2b[4]
- U29 pad 7: /cin[4] -> /rs1b[7]
- U29 pad 8: Net-(U25-Pad12) -> /rs1b[6]
- U29 pad 9: Net-(U25-Pad11) -> /rs1b[5]
- U3 pad 1: Net-(U3-Pad1) -> /cmp[7]
- U3 pad 10: /BOOT_A[1] -> GNDREF
- U3 pad 11: /BOOT_A[0] -> Net-(U3-Pad11)
- U3 pad 12: Net-(U3-Pad12) -> GNDREF
- U3 pad 13: /CLA_D0 -> GNDREF
- U3 pad 14: /CLA_D1 -> VCC
- U3 pad 2: /BOOT_A[14] -> /rdb[0]
- U3 pad 3: /BOOT_A[12] -> /rdb[0]'
- U3 pad 4: /BOOT_A[7] -> /~BOOT_WR
- U3 pad 5: /BOOT_A[6] -> /~BOOT_ALU_EN
- U3 pad 6: /BOOT_A[5] -> /~BOOT_ALU_WR
- U3 pad 7: /BOOT_A[4] -> GNDREF
- U3 pad 8: /BOOT_A[3] -> Net-(U3-Pad8)
- U3 pad 9: /BOOT_A[2] -> GNDREF
- U30 pad 1: /~BOOT_ALU_EN -> GNDREF
- U30 pad 10: GND -> /rs1b[8]
- U30 pad 11: Net-(U30-Pad11) -> /g[2]
- U30 pad 12: Net-(U30-Pad12) -> /p[2]
- U30 pad 14: Net-(U30-Pad14) -> GNDREF
- U30 pad 15: /rs1b[20] -> Net-(U30-Pad15)
- U30 pad 16: /rs1b[21] -> Net-(U30-Pad16)
- U30 pad 17: /rs1b[22] -> Net-(U30-Pad17)
- U30 pad 18: /rs1b[23] -> Net-(U30-Pad18)
- U30 pad 19: /BOOT_A[15] -> Net-(U30-Pad19)
- U30 pad 2: /rs1b[19] -> GNDREF
- U30 pad 20: /SW_VCC3 -> GNDREF
- U30 pad 3: /rs1b[18] -> /rs2b[11]
- U30 pad 4: /rs1b[17] -> /rs2b[10]
- U30 pad 5: /rs1b[16] -> /rs2b[9]
- U30 pad 6: Net-(U26-Pad14) -> /rs2b[8]
- U30 pad 7: Net-(U26-Pad13) -> /rs1b[11]
- U30 pad 8: Net-(U26-Pad12) -> /rs1b[10]
- U30 pad 9: Net-(U26-Pad11) -> /rs1b[9]
- U31 pad 1: /~BOOT_ALU_EN -> GNDREF
- U31 pad 10: GND -> /rs1b[12]
- U31 pad 11: /rdb[20] -> /g[3]
- U31 pad 12: /rdb[21] -> /p[3]
- U31 pad 13: /rdb[22] -> Net-(U31-Pad13)
- U31 pad 14: /rdb[23] -> GNDREF
- U31 pad 15: /cout[5] -> Net-(U31-Pad15)
- U31 pad 16: /p[5] -> Net-(U31-Pad16)
- U31 pad 17: /g[5] -> Net-(U31-Pad17)
- U31 pad 18: /lt[5] -> Net-(U31-Pad18)
- U31 pad 19: /BOOT_A[15] -> Net-(U31-Pad19)
- U31 pad 2: /lt[4] -> GNDREF
- U31 pad 20: /SW_VCC3 -> GNDREF
- U31 pad 3: /g[4] -> /rs2b[15]
- U31 pad 4: /p[4] -> /rs2b[14]
- U31 pad 5: /cout[4] -> /rs2b[13]
- U31 pad 6: /rdb[19] -> /rs2b[12]
- U31 pad 7: /rdb[18] -> /rs1b[15]
- U31 pad 8: /rdb[17] -> /rs1b[14]
- U31 pad 9: /rdb[16] -> /rs1b[13]
- U32 pad 1: GND -> GNDREF
- U32 pad 10: /rs1b[20] -> /rs1b[16]
- U32 pad 11: /rdb[20] -> /g[4]
- U32 pad 12: /rdb[21] -> /p[4]
- U32 pad 13: /rdb[22] -> Net-(U32-Pad13)
- U32 pad 14: GND -> GNDREF
- U32 pad 15: /rdb[23] -> Net-(U32-Pad15)
- U32 pad 16: /cout[5] -> Net-(U32-Pad16)
- U32 pad 17: /p[5] -> Net-(U32-Pad17)
- U32 pad 18: /g[5] -> Net-(U32-Pad18)
- U32 pad 19: /lt[5] -> Net-(U32-Pad19)
- U32 pad 2: /alu_f[3] -> GNDREF
- U32 pad 20: GND -> GNDREF
- U32 pad 21: /alu_f[1] -> /alu_f[2]
- U32 pad 22: /~alu_oe -> /BOOT_ALU_EN
- U32 pad 23: /alu_f[2] -> /alu_f[3]
- U32 pad 24: /alu_f[0] -> /alu_f[1]
- U32 pad 25: /cin[5] -> /alu_f[0]
- U32 pad 26: GND -> GNDREF
- U32 pad 3: /rs2b[23] -> /rs2b[19]
- U32 pad 4: /rs2b[22] -> /rs2b[18]
- U32 pad 5: /rs2b[21] -> /rs2b[17]
- U32 pad 6: /rs2b[20] -> /rs2b[16]
- U32 pad 7: /rs1b[23] -> /rs1b[19]
- U32 pad 8: /rs1b[22] -> /rs1b[18]
- U32 pad 9: /rs1b[21] -> /rs1b[17]
- U33 pad 1: /~BOOT_ALU_EN -> GNDREF
- U33 pad 10: GND -> /rs1b[20]
- U33 pad 11: Net-(U33-Pad11) -> /g[5]
- U33 pad 12: Net-(U33-Pad12) -> /p[5]
- U33 pad 13: /cin[6] -> Net-(U33-Pad13)
- U33 pad 14: Net-(U33-Pad14) -> GNDREF
- U33 pad 15: /rs2b[27] -> Net-(U33-Pad15)
- U33 pad 16: /rs2b[26] -> Net-(U33-Pad16)
- U33 pad 17: /rs2b[25] -> Net-(U33-Pad17)
- U33 pad 18: /rs2b[24] -> Net-(U33-Pad18)
- U33 pad 19: /BOOT_A[15] -> Net-(U33-Pad19)
- U33 pad 2: /rs2b[20] -> GNDREF
- U33 pad 20: /SW_VCC3 -> GNDREF
- U33 pad 3: /rs2b[21] -> /rs2b[23]
- U33 pad 5: /rs2b[23] -> /rs2b[21]
- U33 pad 6: Net-(U29-Pad14) -> /rs2b[20]
- U33 pad 7: /cin[5] -> /rs1b[23]
- U33 pad 8: Net-(U29-Pad12) -> /rs1b[22]
- U33 pad 9: Net-(U29-Pad11) -> /rs1b[21]
- U34 pad 1: /~BOOT_ALU_EN -> GNDREF
- U34 pad 10: GND -> /rs1b[24]
- U34 pad 11: Net-(U34-Pad11) -> /g[6]
- U34 pad 12: Net-(U34-Pad12) -> /p[6]
- U34 pad 14: Net-(U34-Pad14) -> GNDREF
- U34 pad 15: /rs1b[24] -> Net-(U34-Pad15)
- U34 pad 16: /rs1b[25] -> Net-(U34-Pad16)
- U34 pad 17: /rs1b[26] -> Net-(U34-Pad17)
- U34 pad 18: /rs1b[27] -> Net-(U34-Pad18)
- U34 pad 19: /BOOT_A[15] -> Net-(U34-Pad19)
- U34 pad 2: /rs1b[23] -> GNDREF
- U34 pad 20: /SW_VCC3 -> GNDREF
- U34 pad 3: /rs1b[22] -> /rs2b[27]
- U34 pad 4: /rs1b[21] -> /rs2b[26]
- U34 pad 5: /rs1b[20] -> /rs2b[25]
- U34 pad 6: Net-(U30-Pad14) -> /rs2b[24]
- U34 pad 7: Net-(U30-Pad13) -> /rs1b[27]
- U34 pad 8: Net-(U30-Pad12) -> /rs1b[26]
- U34 pad 9: Net-(U30-Pad11) -> /rs1b[25]
- U35 pad 1: /~BOOT_ALU_EN -> Net-(U35-Pad1)
- U35 pad 10: GND -> /BOOT_A[1]
- U35 pad 11: /rdb[24] -> /BOOT_A[0]
- U35 pad 12: /rdb[25] -> Net-(U35-Pad12)
- U35 pad 13: /rdb[26] -> /CLU_D0
- U35 pad 14: /rdb[27] -> /CLU_D1
- U35 pad 15: /cout[6] -> /CLU_D2
- U35 pad 16: /p[6] -> GNDREF
- U35 pad 17: /g[6] -> Net-(U35-Pad17)
- U35 pad 18: /lt[6] -> /CLU_D3
- U35 pad 19: /BOOT_A[15] -> /CLU_D4
- U35 pad 2: /lt[5] -> /BOOT_A[14]
- U35 pad 20: /SW_VCC3 -> /CLU_D5
- U35 pad 3: /g[5] -> /BOOT_A[12]
- U35 pad 4: /p[5] -> /BOOT_A[7]
- U35 pad 5: /cout[5] -> /BOOT_A[6]
- U35 pad 6: /rdb[23] -> /BOOT_A[5]
- U35 pad 7: /rdb[22] -> /BOOT_A[4]
- U35 pad 8: /rdb[21] -> /BOOT_A[3]
- U35 pad 9: /rdb[20] -> /BOOT_A[2]
- U36 pad 1: GND -> Net-(U36-Pad1)
- U36 pad 10: /rs1b[24] -> /BOOT_A[1]
- U36 pad 11: /rdb[24] -> /BOOT_A[0]
- U36 pad 12: /rdb[25] -> Net-(U36-Pad12)
- U36 pad 13: /rdb[26] -> /SLICE2_D[0]
- U36 pad 14: GND -> /SLICE2_D[1]
- U36 pad 15: /rdb[27] -> /SLICE2_D[2]
- U36 pad 16: /cout[6] -> GNDREF
- U36 pad 17: /p[6] -> Net-(U36-Pad17)
- U36 pad 18: /g[6] -> /SLICE2_D[3]
- U36 pad 19: /lt[6] -> /SLICE2_D[4]
- U36 pad 2: /alu_f[3] -> Net-(U36-Pad2)
- U36 pad 20: GND -> Net-(U36-Pad20)
- U36 pad 21: /alu_f[1] -> Net-(U36-Pad21)
- U36 pad 22: /~alu_oe -> Net-(U36-Pad22)
- U36 pad 23: /alu_f[2] -> GNDREF
- U36 pad 24: /alu_f[0] -> /BOOT_A[10]
- U36 pad 25: /cin[6] -> GNDREF
- U36 pad 26: GND -> Net-(U36-Pad26)
- U36 pad 27: /~BOOT_ALU_WR -> /BOOT_A[11]
- U36 pad 28: VCC -> /BOOT_A[9]
- U36 pad 3: /rs2b[27] -> /BOOT_A[12]
- U36 pad 4: /rs2b[26] -> /BOOT_A[7]
- U36 pad 5: /rs2b[25] -> /BOOT_A[6]
- U36 pad 6: /rs2b[24] -> /BOOT_A[5]
- U36 pad 7: /rs1b[27] -> /BOOT_A[4]
- U36 pad 8: /rs1b[26] -> /BOOT_A[3]
- U36 pad 9: /rs1b[25] -> /BOOT_A[2]
- U37 pad 10: GND -> GNDREF
- U37 pad 12: Net-(U37-Pad12) -> /cin[7]
- U37 pad 13: /cin[7] -> /cin[6]
- U37 pad 14: Net-(U37-Pad14) -> /cin[5]
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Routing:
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- added copper zone on In1.Cu, net GNDREF
- removed copper zone on In1.Cu, net GND
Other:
- board size 111.3 x 141 mm -> 158 x 115.2 mm
- board text added: "BITSLICE ROM"
- board text added: "BOOT_ALU_EN"
- board text added: "CLU ROM"
- board text added: "LMARV-1 ARITHMETIC LOGIC UNIT REV B 2008 OCT 21"
- board text added: "PROPAGATE/GENERATE ROM"
- board text removed: "/BOOT_CLA_WR"
- board text removed: "ALU SLICE ROM"
- board text removed: "CLA ROM"
- board text removed: "LMARV-1 ARITHMETIC LOGIC UNIT REV B 2018 JUL 7"
- board text removed: "SW_VCC1"
- board text removed: "SW_VCC2"
- board text removed: "SW_VCC3"

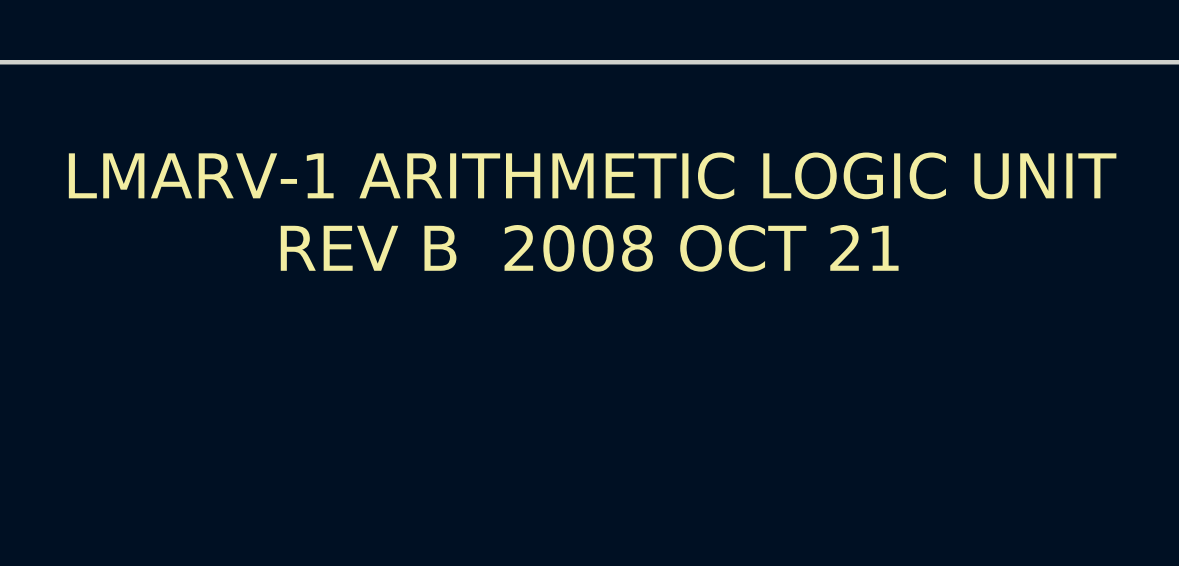
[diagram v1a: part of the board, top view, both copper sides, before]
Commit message: Updated ALU, tester, more instruction pages
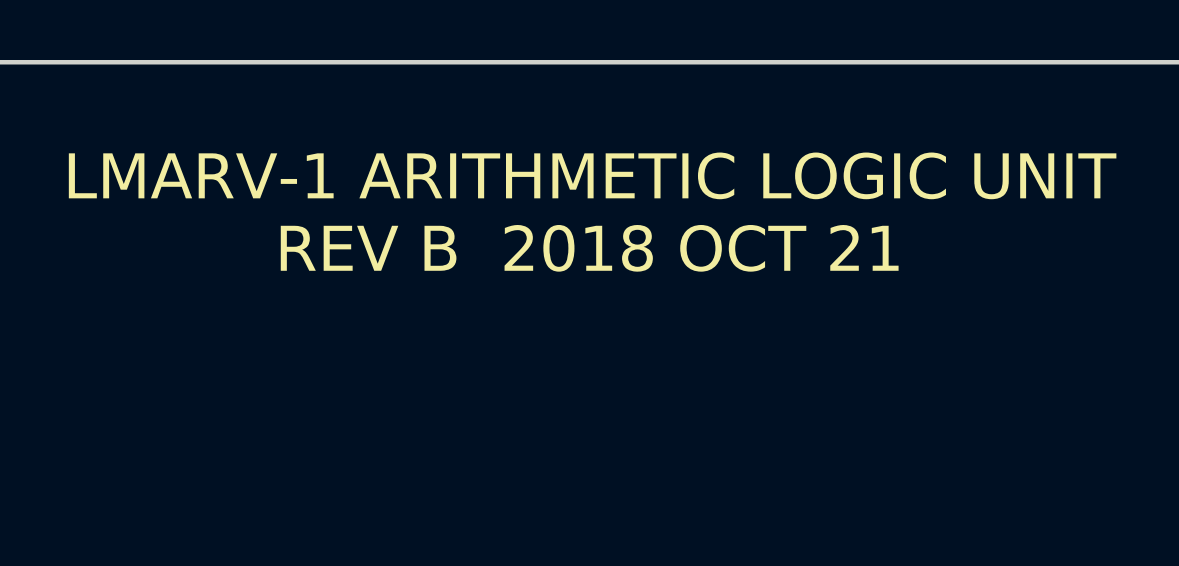
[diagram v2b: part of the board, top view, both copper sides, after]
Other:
- board text added: "LMARV-1 ARITHMETIC LOGIC UNIT REV B 2018 OCT 21"
- board text removed: "LMARV-1 ARITHMETIC LOGIC UNIT REV B 2008 OCT 21"
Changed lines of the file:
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@@
     (effects (font (size 1.5 1.5) (thickness 0.3)))
   )
-  (gr_text "LMARV-1 ARITHMETIC LOGIC UNIT\nREV B  2008 OCT 21" (at 85.15 35.05) (layer F.SilkS)
+  (gr_text "LMARV-1 ARITHMETIC LOGIC UNIT\nREV B  2018 OCT 21" (at 85.15 35.05) (layer F.SilkS)
     (effects (font (size 1.5 1.5) (thickness 0.3)))
   )
@@
   (segment (start 168.95 102.512836) (end 168.95 103.434315) (width 0.178) (layer F.Cu) (net 180))
   (segment (start 168.65568 93.081291) (end 168.65568 94.251635) (width 0.178) (layer F.Cu) (net 180))
-  (via (at 209.625 128.7) (size 0.8) (drill 0.4) (layers F.Cu B.Cu) (net 440))
-  (segment (start 88.45 112.440882) (end 88.277976 112.268858) (width 0.178) (layer B.Cu) (net 440))
-  (via (at 88.277976 112.268858) (size 0.8) (drill 0.4) (layers F.Cu B.Cu) (net 440))
-  (segment (start 88.45 113.5) (end 88.45 112.440882) (width 0.178) (layer B.Cu) (net 440) (status 10))
-  (segment (start 212.05 117.95) (end 212.05 119.203231) (width 0.178) (layer F.Cu) (net 440))
-  (segment (start 212.05 119.203231) (end 211.751615 119.501616) (width 0.178) (layer F.Cu) (net 440))
-  (segment (start 209.625 128.7) (end 211.751615 126.573385) (width 0.178) (layer B.Cu) (net 440))
-  (segment (start 211.751615 120.067301) (end 211.751615 119.501616) (width 0.178) (layer B.Cu) (net 440))
-  (segment (start 211.751615 126.573385) (end 211.751615 120.067301) (width 0.178) (layer B.Cu) (net 440))
-  (via (at 211.751615 119.501616) (size 0.8) (drill 0.4) (layers F.Cu B.Cu) (net 440))
   (segment (start 213.025 126.147) (end 217.1 122.072) (width 0.178) (layer F.Cu) (net 182))
   (segment (start 213.025 127.05) (end 213.025 126.147) (width 0.178) (layer F.Cu) (net 182) (status 10))
@@
   (segment (start 79.675 103.147) (end 76.304499 99.776499) (width 0.178) (layer F.Cu) (net 396))
   (segment (start 79.675 104.05) (end 79.675 103.147) (width 0.178) (layer F.Cu) (net 396) (status 10))
+  (via (at 209.625 128.7) (size 0.8) (drill 0.4) (layers F.Cu B.Cu) (net 440))
+  (segment (start 88.45 112.440882) (end 88.277976 112.268858) (width 0.178) (layer B.Cu) (net 440))
+  (via (at 88.277976 112.268858) (size 0.8) (drill 0.4) (layers F.Cu B.Cu) (net 440))
+  (segment (start 88.45 113.5) (end 88.45 112.440882) (width 0.178) (layer B.Cu) (net 440) (status 10))
+  (segment (start 212.05 117.95) (end 212.05 119.203231) (width 0.178) (layer F.Cu) (net 440))
+  (segment (start 212.05 119.203231) (end 211.751615 119.501616) (width 0.178) (layer F.Cu) (net 440))
+  (segment (start 209.625 128.7) (end 211.751615 126.573385) (width 0.178) (layer B.Cu) (net 440))
+  (segment (start 211.751615 120.067301) (end 211.751615 119.501616) (width 0.178) (layer B.Cu) (net 440))
+  (segment (start 211.751615 126.573385) (end 211.751615 120.067301) (width 0.178) (layer B.Cu) (net 440))
+  (via (at 211.751615 119.501616) (size 0.8) (drill 0.4) (layers F.Cu B.Cu) (net 440))
   (segment (start 117.504166 129.217002) (end 125.720834 129.217002) (width 0.178) (layer B.Cu) (net 440))
   (segment (start 88.45 113.5) (end 88.45 114.245355) (width 0.178) (layer B.Cu) (net 440))
